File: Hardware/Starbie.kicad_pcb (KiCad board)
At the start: 2 copper layers, 97.7 x 82.6 mm, 14 parts, among them J1 Conn_01x04_Pin, J2 Conn_01x08_Pin, SW1 SW_Push, SW2 SW_Push, U1 DHT11, U2 XIAO-ESP32-C3-SMD

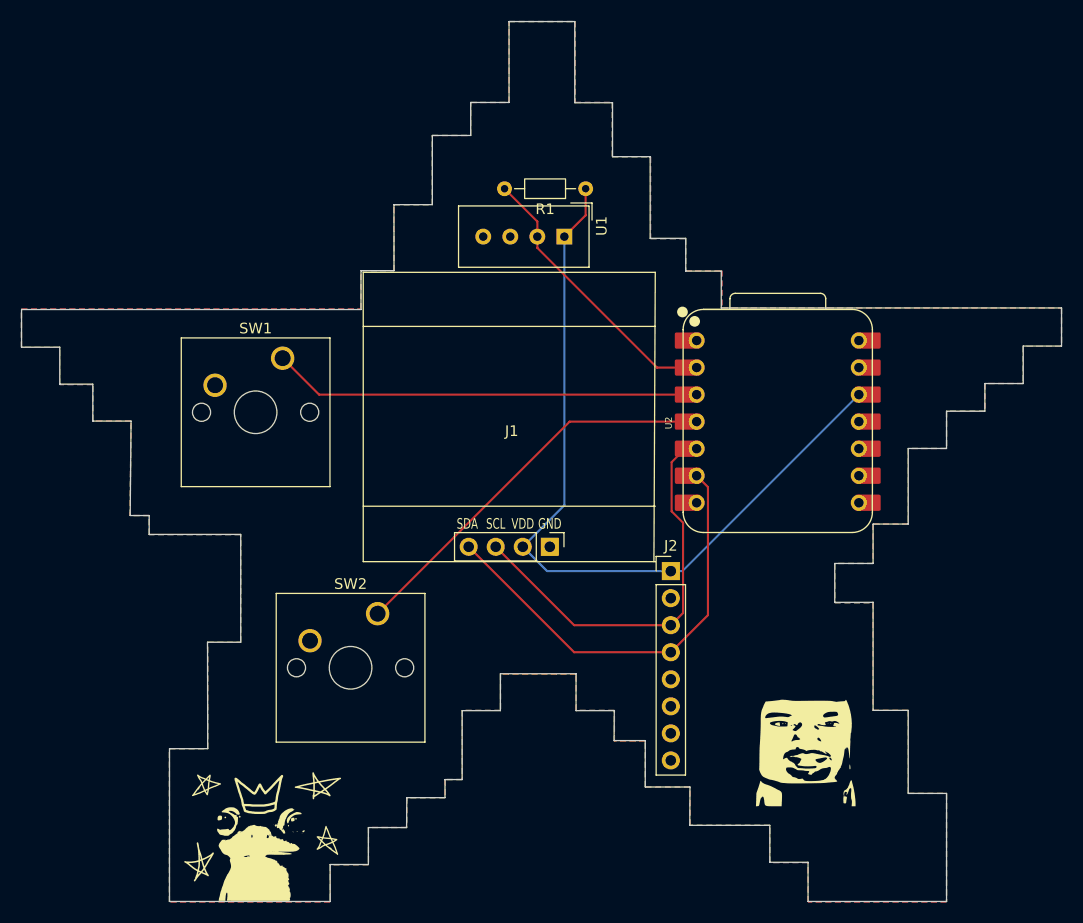
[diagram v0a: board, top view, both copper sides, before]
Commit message: Update Gerber files after PCB layer edits
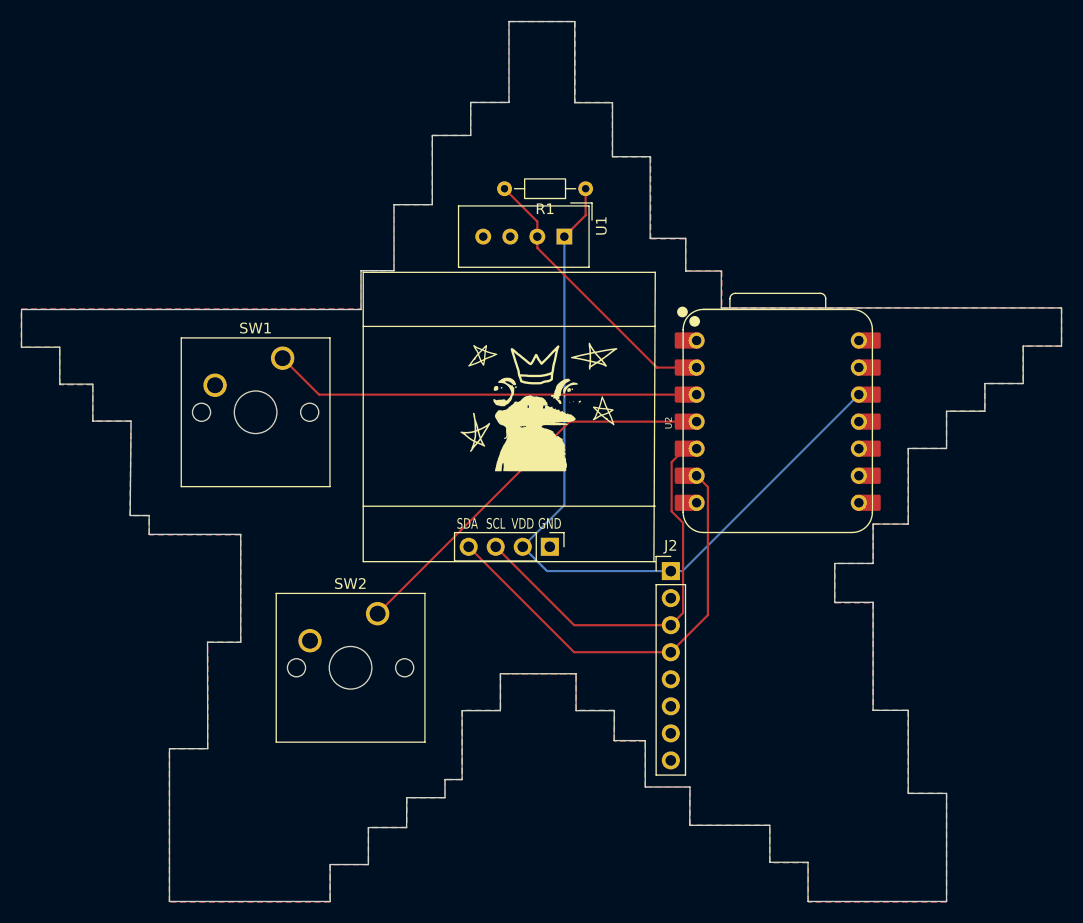
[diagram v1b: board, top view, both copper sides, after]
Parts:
- removed the G*** at (180.1, 116.6)
- moved G*** 48.0 mm to (148.2, 89.7)
- moved G*** 48.0 mm to (153.4, 83.3)
- moved G*** 48.0 mm to (160.8, 87.0)
- moved G*** 48.0 mm to (149.2, 82.8)
- moved G*** 48.0 mm to (154.2, 87.0)
- moved G*** 48.0 mm to (159.2, 82.9)
